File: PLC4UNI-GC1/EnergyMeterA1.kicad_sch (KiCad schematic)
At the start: 23 parts, among them U16 BL0942, U17 B0303S-1WR3_C7465185, U18 ISO7021DR

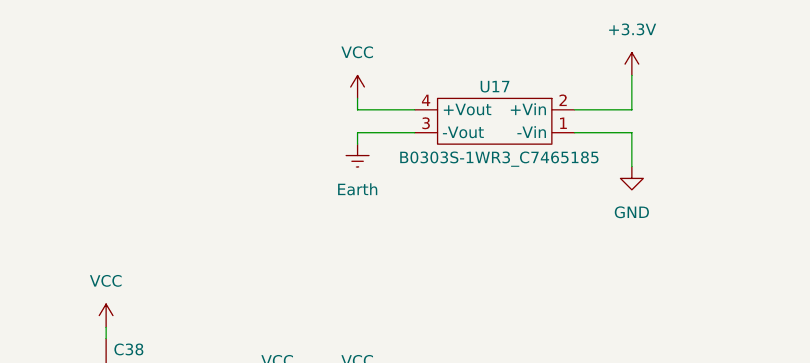
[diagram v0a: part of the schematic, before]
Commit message: Colocadas el 80% de las piezas
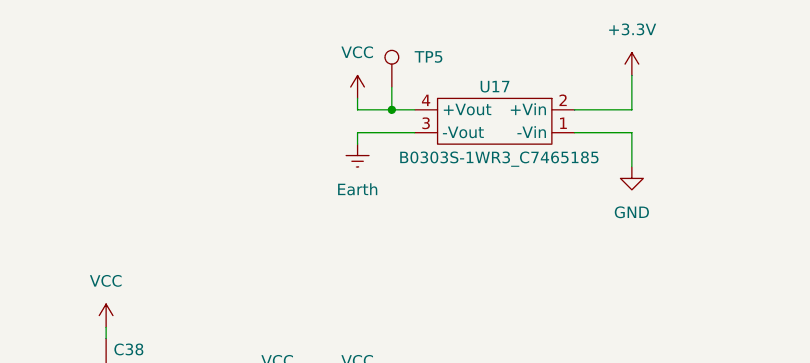
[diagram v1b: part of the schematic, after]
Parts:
- added TP5: TestPoint_Hole1, 4ms_TestPoint:TestPoint_WireHole, symbol MG_ELECTROMECANICAL:TestPoint_Hole1
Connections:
- net VCC: now also TP5.1
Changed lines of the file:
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@@
 	)
 	(junction
+		(at 171.45 36.83)
+		(diameter 0)
+		(color 0 0 0 0)
+	)
+	(junction
 		(at 96.52 115.57)
 		(diameter 0)
@@
 	(wire
 		(pts
+			(xy 171.45 34.29) (xy 171.45 36.83)
+		)
+		(stroke
+			(width 0)
+			(type default)
+		)
+	)
+	(wire
+		(pts
 			(xy 46.99 115.57) (xy 49.53 115.57)
 		)
@@
 	(wire
 		(pts
+			(xy 171.45 36.83) (xy 167.64 36.83)
+		)
+		(stroke
+			(width 0)
+			(type default)
+		)
+	)
+	(wire
+		(pts
 			(xy 96.52 115.57) (xy 87.63 115.57)
 		)
@@
 	(wire
 		(pts
-			(xy 173.99 36.83) (xy 167.64 36.83)
+			(xy 173.99 36.83) (xy 171.45 36.83)
 		)
 		(stroke
@@
 					(unit 1)
 				)
+			)
+		)
+	)
+	(symbol
+		(lib_id "MG_ELECTROMECANICAL:TestPoint_Hole1")
+		(at 171.45 34.29 0)
+		(unit 1)
+		(exclude_from_sim no)
+		(in_bom yes)
+		(on_board yes)
+		(dnp no)
+		(fields_autoplaced yes)
+		(property "Reference" "TP5"
+			(at 173.99 30.9879 0)
+			(effects
+				(font
+					(size 1.27 1.27)
+				)
+				(justify left)
+			)
+		)
+		(property "Value" "TestPoint_Hole1"
+			(at 171.45 29.21 0)
+			(effects
+				(font
+					(size 1.27 1.27)
+				)
+				(hide yes)
+			)
+		)
+		(property "Footprint" "4ms_TestPoint:TestPoint_WireHole"
+			(at 176.53 34.29 0)
+			(effects
+				(font
+					(size 1.27 1.27)
+				)
+				(hide yes)
+			)
+		)
+		(property "Datasheet" "~"
+			(at 176.53 34.29 0)
+			(effects
+				(font
+					(size 1.27 1.27)
+				)
+				(hide yes)
+			)
+		)
+		(property "Description" "test point"
+			(at 171.45 34.29 0)
+			(effects
+				(font
+					(size 1.27 1.27)
+				)
+				(hide yes)
+			)
+		)
+		(pin "1"
+		)
+		(instances
+			(project "PLC4UNI-GC1"
+				(path "/78be00cd-daf6-4f2a-9977-d3085e20b798/ca21e56d-4223-44eb-9b60-6c8fe421c362/ca73a3a2-e972-4904-8497-8f601585c9f2"
+					(reference "TP5")
+					(unit 1)
+				)

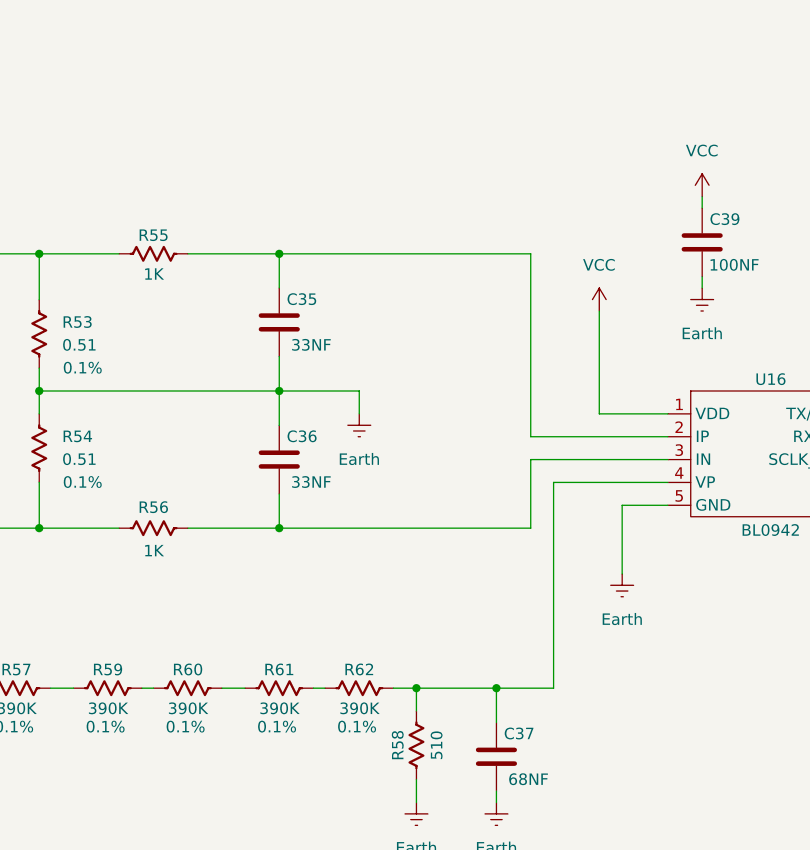
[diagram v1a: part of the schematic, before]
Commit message: Avances en colocacion de piezas y verificacion de componentes
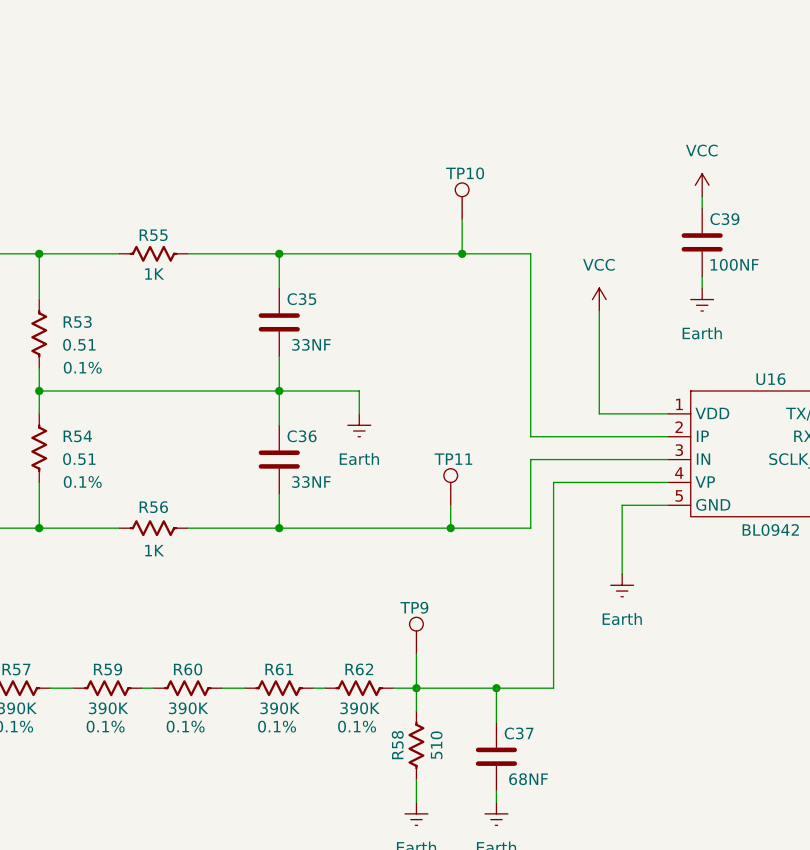
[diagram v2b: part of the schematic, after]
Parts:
- added TP10, TP11, TP9: TestPoint_Hole1, 4ms_TestPoint:TestPoint_WireHole, symbol MG_ELECTROMECANICAL:TestPoint_Hole1
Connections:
- net at C36.1, R56.2, U16.3 (IN): now also TP11.1
- net at C37.2, R58.2, R62.2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: now also TP9.1
- net at C35.2, R55.2, U16.2 (IP): now also TP10.1
